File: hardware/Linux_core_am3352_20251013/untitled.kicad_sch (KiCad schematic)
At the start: 1 part, among them U1 AM3352BZCZ100

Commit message: update
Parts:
- removed U1: AM3352BZCZ100, My_Library:ZCZ0324A, symbol My_Library:AM3352BZCZ100
- added C1, C2: 18pF, symbol Device:C_Small
- added C3, C4: 22pF, symbol Device:C_Small
- added R1: R_Small, symbol Device:R_Small
- added R2, R3: 0Ω, symbol Device:R_Small
- added U1: AM3352BZCZ100, My_Library:ZCZ0324A, symbol My_Library:AM3352BZCZ100
- added Y1: 24MHz, Oscillator:Oscillator_SMD_Abracon_ASCO-4Pin_1.6x1.2mm, symbol Device:Crystal_GND24_Small
- added Y2: 32.768KHz, symbol Device:Crystal_Small
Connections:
- new net: C4.2, R3.1, Y2.1
- new net: C3.2, U1.A6 (RTC_XTALIN), Y2.2
- new net: C2.2, R1.2, R2.1, Y1.1
- new net: C1.2, R1.1, U1.V10 (XTALIN), Y1.3
- new net: R2.2, U1.U11 (XTALOUT)
- new net: R3.2, U1.A4 (RTC_XTALOUT)
- new net GND_OSC0: C1.1, C2.1, C3.1, C4.1, U1.A5 (VSS_RTC), U1.V11 (VSS_OSC)
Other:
- removed sheet am3352_a
- note added: "确认晶振接地方案"

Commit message: update
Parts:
- added C5: 0.1uF, symbol Device:C_Small
- added R4: 49.9Ω, symbol Device:R_Small
- added R5: 100KΩ, symbol Device:R_Small
- added R6, R7, R8: 10KΩ, symbol Device:R_Small
- added R9: 22Ω, symbol Device:R_Small
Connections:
- net at U1.A10 (WARMRST_N): now also R6.1
- net JTAG_TDO: now reaches U1.A11 (TDO)
- net JTAG_TCK: now reaches U1.A12 (TCK)
- net at U1.A15 (XDMA_EVENT_INTR0): now also R7.2
- net DDR_A5: now reaches U1.B1 (DDR_A5)
- net JTAG_TRST_N: now reaches U1.B10 (TRST_N)
- net JTAG_TDI: now reaches U1.B11 (TDI)
- net JTAG_EMU1: now reaches U1.B14 (EMU1)
- net PWRONRST_N: now reaches U1.B15 (PWRONRST_N)
- net PWRONRST_N: now also R5.2
- net EXTINT_N: now reaches U1.B18 (EXTINT_N)
- net DDR_WEn: now reaches U1.B2 (DDR_WE_N)
- net DDR_BA2: now reaches U1.B3 (DDR_BA2)
- net RTC_PORz: now reaches U1.B5 (RTC_PWRONRST_N)
- net DDR_A9: now reaches U1.C1 (DDR_A9)
- net JTAG_TMS: now reaches U1.C11 (TMS)
- net JTAG_EMU0: now reaches U1.C14 (EMU0)
- net DDR_A4: now reaches U1.C2 (DDR_A4)
- net DDR_A3: now reaches U1.C3 (DDR_A3)
- net DDR_BA0: now reaches U1.C4 (DDR_BA0)
- net DDR_CKn: now reaches U1.D1 (DDR_CK_N)
- net at U1.D14 (XDMA_EVENT_INTR1): now also R8.2
- net DDR_CK: now reaches U1.D2 (DDR_CK)
- net DDR_A15: now reaches U1.D3 (DDR_A15)
- net DDR_A8: now reaches U1.D4 (DDR_A8)
- net DDR_A6: now reaches U1.D5 (DDR_A6)
- net DDR_BA1: now reaches U1.E1 (DDR_BA1)
- net DDR_A7: now reaches U1.E2 (DDR_A7)
- net DDR_A12: now reaches U1.E3 (DDR_A12)
- net DDR_A2: now reaches U1.E4 (DDR_A2)
- net DDR_CASn: now reaches U1.F1 (DDR_CAS_N)
- net MMC0_DAT3: now reaches U1.F17 (MMC0_DAT3)
- net MMC0_DAT2: now reaches U1.F18 (MMC0_DAT2)
- net DDR_A11: now reaches U1.F2 (DDR_A11)
- net DDR_A0: now reaches U1.F3 (DDR_A0)
- net DDR_A10: now reaches U1.F4 (DDR_A10)
- net DDR_ODT: now reaches U1.G1 (DDR_ODT)
- net MMC0_DAT1: now reaches U1.G15 (MMC0_DAT1)
- net MMC0_DAT0: now reaches U1.G16 (MMC0_DAT0)
- net MMC0_CLK: now reaches U1.G17 (MMC0_CLK)
- net at U1.G18 (MMC0_CMD): now also R9.2
- net DDR_RESETn: now reaches U1.G2 (DDR_RESET_N)
- net DDR_CKE: now reaches U1.G3 (DDR_CKE)
- net DDR_RASn: now reaches U1.G4 (DDR_RAS_N)
- net DDR_A1: now reaches U1.H1 (DDR_A1)
- net DDR_CSn0: now reaches U1.H2 (DDR_CS0_N)
- net DDR_A13: now reaches U1.H3 (DDR_A13)
- net DDR_A14: now reaches U1.H4 (DDR_A14)
- net DDR_D8: now reaches U1.J1 (DDR_D8)
- net DDR_DQM1: now reaches U1.J2 (DDR_DQM1)
- net at U1.J3 (DDR_VTP): now also R4.2
- net DDR_VREF: now reaches U1.J4 (DDR_VREF)
- net DDR_VREF: now also C5.2
- net DDR_D9: now reaches U1.K1 (DDR_D9)
- net DDR_D10: now reaches U1.K2 (DDR_D10)
- net DDR_D11: now reaches U1.K3 (DDR_D11)
- net DDR_D12: now reaches U1.K4 (DDR_D12)
- net DDR_DQS1: now reaches U1.L1 (DDR_DQS1)
- net DDR_DQSn1: now reaches U1.L2 (DDR_DQS1_N)
- net DDR_D13: now reaches U1.L3 (DDR_D13)
- net DDR_D14: now reaches U1.L4 (DDR_D14)
- net DDR_D15: now reaches U1.M1 (DDR_D15)
- net DDR_DQM0: now reaches U1.M2 (DDR_DQM0)
- net DDR_D0: now reaches U1.M3 (DDR_D0)
- net DDR_D1: now reaches U1.M4 (DDR_D1)
- net DDR_D2: now reaches U1.N1 (DDR_D2)
- net DDR_D3: now reaches U1.N2 (DDR_D3)
- net DDR_D4: now reaches U1.N3 (DDR_D4)
- net DDR_D5: now reaches U1.N4 (DDR_D5)
- net DDR_DQS0: now reaches U1.P1 (DDR_DQS0)
- net DDR_DQSn0: now reaches U1.P2 (DDR_DQS0_N)
- net DDR_D6: now reaches U1.P3 (DDR_D6)
- net DDR_D7: now reaches U1.P4 (DDR_D7)
- net GPMC_AD13: now reaches U1.R12 (GPMC_AD13)
- net GPMC_A0: now reaches U1.R13 (GPMC_A0)
- net GPMC_A4: now reaches U1.R14 (GPMC_A4)
- net GPMC_ADV_ALE_N: now reaches U1.R7 (GPMC_ADV_ALE_N)
- net GPMC_AD2: now reaches U1.R8 (GPMC_AD2)
- net GPMC_AD6: now reaches U1.R9 (GPMC_AD6)
- net GPMC_AD9: now reaches U1.T10 (GPMC_AD9)
- net GPMC_AD10: now reaches U1.T11 (GPMC_AD10)
- net GPMC_AD12: now reaches U1.T12 (GPMC_AD12)
- net GPMC_CS3_N: now reaches U1.T13 (GPMC_CS3_N)
- net GPMC_A3: now reaches U1.T14 (GPMC_A3)
- net GPMC_A7: now reaches U1.T15 (GPMC_A7)
- net GPMC_A10: now reaches U1.T16 (GPMC_A10)
- net GPMC_WAIT0: now reaches U1.T17 (GPMC_WAIT0)
- net GPMC_BE0_CLE_N: now reaches U1.T6 (GPMC_BE0_CLE_N)
- net GPMC_OEN_RE_N: now reaches U1.T7 (GPMC_OEN_RE_N)
- net GPMC_AD3: now reaches U1.T8 (GPMC_AD3)
- net GPMC_AD7: now reaches U1.T9 (GPMC_AD7)
- net GPMC_AD8: now reaches U1.U10 (GPMC_AD8)
- net GPMC_AD11: now reaches U1.U12 (GPMC_AD11)
- net GPMC_AD15: now reaches U1.U13 (GPMC_AD15)
- net GPMC_A2: now reaches U1.U14 (GPMC_A2)
- net GPMC_A6: now reaches U1.U15 (GPMC_A6)
- net GPMC_A9: now reaches U1.U16 (GPMC_A9)
- net GPMC_WP_N: now reaches U1.U17 (GPMC_WP_N)
- net GPMC_BE1_N: now reaches U1.U18 (GPMC_BE1_N)
- net GPMC_WE_N: now reaches U1.U6 (GPMC_WE_N)
- net GPMC_AD0: now reaches U1.U7 (GPMC_AD0)
- net GPMC_AD4: now reaches U1.U8 (GPMC_AD4)
- net GPMC_CS1_N: now reaches U1.U9 (GPMC_CS1_N)
- net GPMC_CLK: now reaches U1.V12 (GPMC_CLK)
- net GPMC_AD14: now reaches U1.V13 (GPMC_AD14)
- net GPMC_A1: now reaches U1.V14 (GPMC_A1)
- net GPMC_A5: now reaches U1.V15 (GPMC_A5)
- net GPMC_A8: now reaches U1.V16 (GPMC_A8)
- net GPMC_A11: now reaches U1.V17 (GPMC_A11)
- net GPMC_CS0_N: now reaches U1.V6 (GPMC_CS0_N)
- net GPMC_AD1: now reaches U1.V7 (GPMC_AD1)
- net GPMC_AD5: now reaches U1.V8 (GPMC_AD5)
- net GPMC_CS2_N: now reaches U1.V9 (GPMC_CS2_N)
- new net GND: C5.1, R4.1, R5.1
- new net MMC0_CMD: R9.1
- new net VDDSHV6: R6.2
- new net XDMA_EVENT_INTR0: R7.1
- new net XDMA_EVENT_INTR1: R8.1
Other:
- moved on the sheet: C1, C2, C3, C4, R1, R2, R3, U1A, Y1, Y2

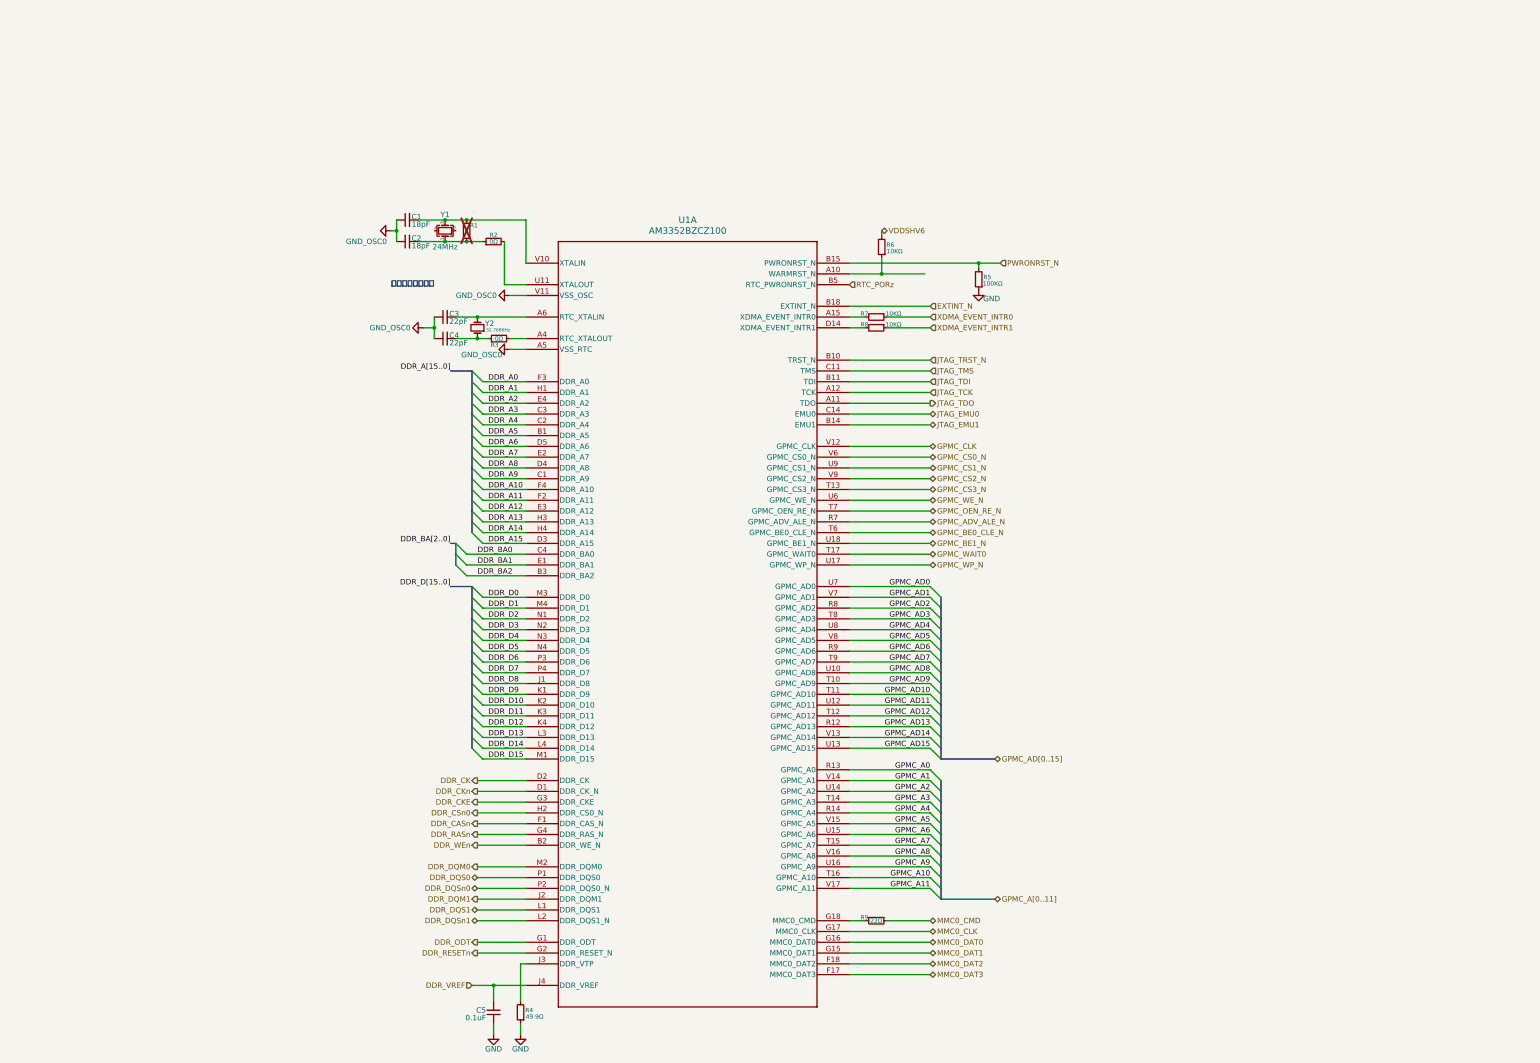
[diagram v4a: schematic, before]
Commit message: update schematic diagram
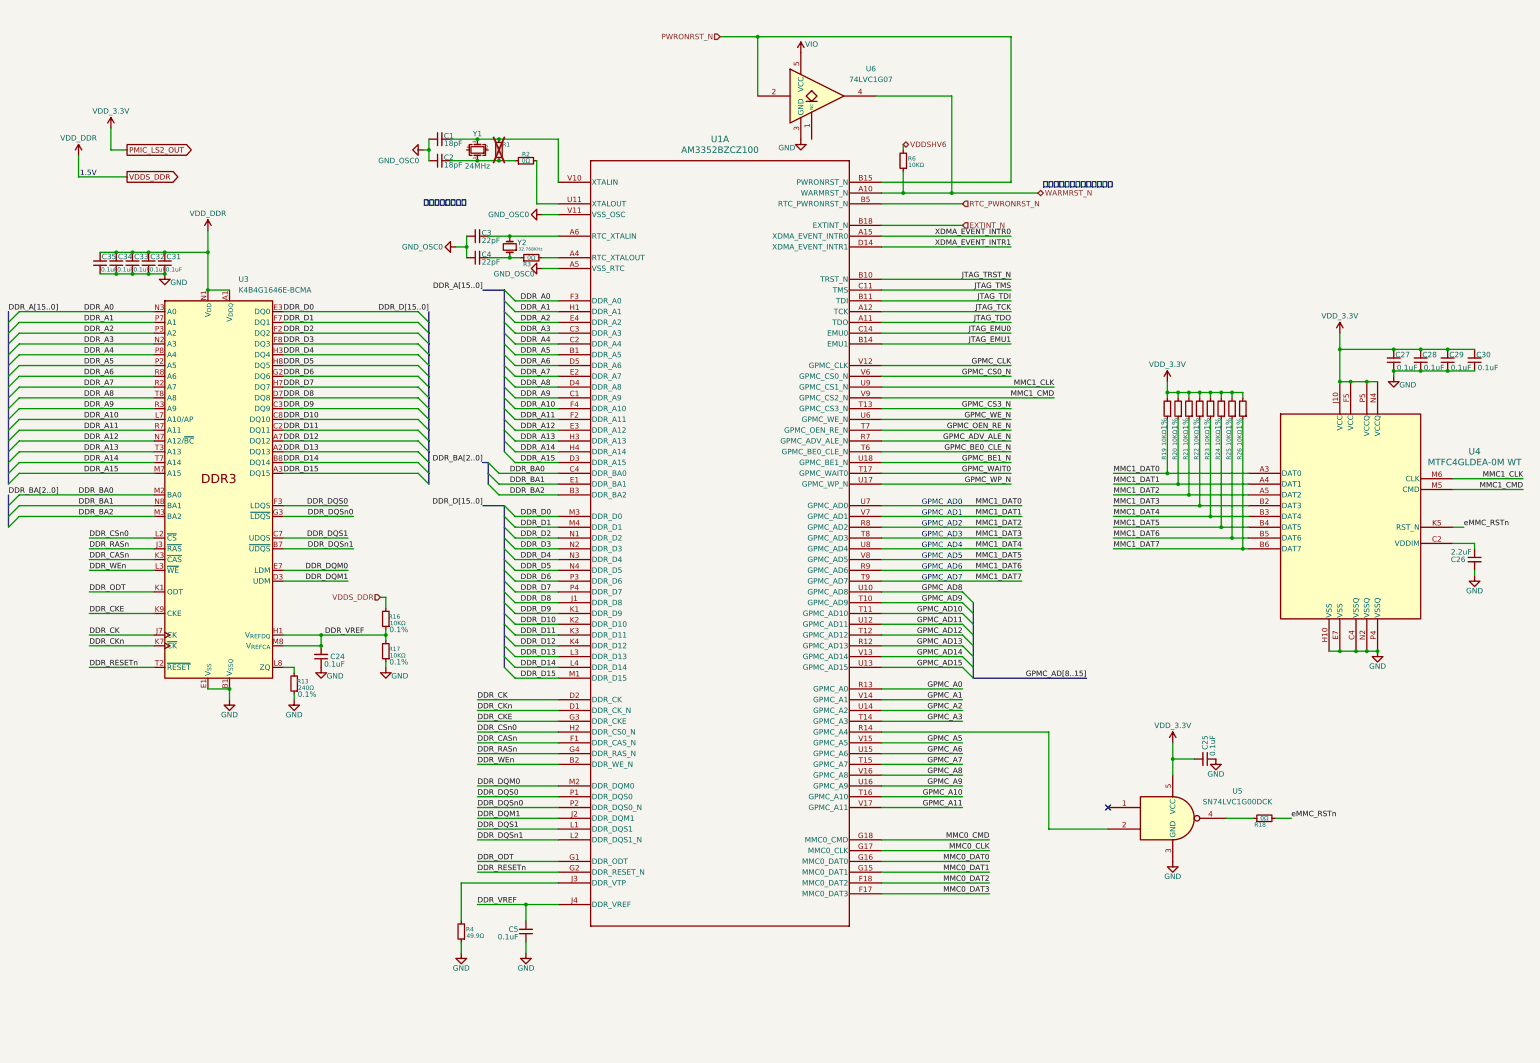
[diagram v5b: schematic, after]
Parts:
- removed R5: 100KΩ, symbol Device:R_Small
- removed R7, R8: 10KΩ, symbol Device:R_Small
- removed R9: 22Ω, symbol Device:R_Small
- added C24, C25, C27, C28, C29, C30, C31, C32, C33, C34, C35: 0.1uF, symbol Device:C_Small
- added C26: 2.2uF, symbol Device:C_Small
- added R13: 240Ω, symbol Device:R_Small
- added R16, R17, R19, R20, R21, R22, R23, R24, R25, R26: 10KΩ, symbol Device:R_Small
- added R18: 0Ω, symbol Device:R_Small
- added U3: K4B4G1646E-BCMA, Package_BGA:Micron_FBGA-96_7.5x13.5mm_Layout9x16_P0.8mm, symbol My_Library:K4B4G1646E
- added U4: MTFC4GLDEA-0M WT, Package_BGA:LFBGA-153_11.5x13mm_Layout14x14_P0.5mm, symbol My_Library:MTFC4GLDEA-0M_WT
- added U5: SN74LVC1G00DCK, Package_TO_SOT_SMD:Texas_R-PDSO-G5_DCK-5, symbol 74xGxx:SN74LVC1G00DCK
- added U6: 74LVC1G07, symbol 74xGxx:74LVC1G07
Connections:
- net DDR_A0: now also U3.N3 (A0)
- net DDR_A1: now also U3.P7 (A1)
- net DDR_A10: now also U3.L7 (A10/AP)
- net DDR_A11: now also U3.R7 (A11)
- net DDR_A12: now also U3.N7 (A12/~{BC})
- net DDR_A13: now also U3.T3 (A13)
- net DDR_A14: now also U3.T7 (A14)
- net DDR_A15: now also U3.M7 (A15)
- net DDR_A2: now also U3.P3 (A2)
- net DDR_A3: now also U3.N2 (A3)
- net DDR_A4: now also U3.P8 (A4)
- net DDR_A5: now also U3.P2 (A5)
- net DDR_A6: now also U3.R8 (A6)
- net DDR_A7: now also U3.R2 (A7)
- net DDR_A8: now also U3.T8 (A8)
- net DDR_A9: now also U3.R3 (A9)
- net DDR_BA0: now also U3.M2 (BA0)
- net DDR_BA1: now also U3.N8 (BA1)
- net DDR_BA2: now also U3.M3 (BA2)
- net DDR_CASn: now also U3.K3 (~{CAS})
- net DDR_CK: now also U3.J7 (CK)
- net DDR_CKE: now also U3.K9 (CKE)
- net DDR_CKn: now also U3.K7 (~{CK})
- net DDR_CSn0: now also U3.L2 (~{CS})
- net DDR_D0: now also U3.E3 (DQ0)
- net DDR_D1: now also U3.F7 (DQ1)
- net DDR_D10: now also U3.C8 (DQ10)
- net DDR_D11: now also U3.C2 (DQ11)
- net DDR_D12: now also U3.A7 (DQ12)
- net DDR_D13: now also U3.A2 (DQ13)
- net DDR_D14: now also U3.B8 (DQ14)
- net DDR_D15: now also U3.A3 (DQ15)
- net DDR_D2: now also U3.F2 (DQ2)
- net DDR_D3: now also U3.F8 (DQ3)
- net DDR_D4: now also U3.H3 (DQ4)
- net DDR_D5: now also U3.H8 (DQ5)
- net DDR_D6: now also U3.G2 (DQ6)
- net DDR_D7: now also U3.H7 (DQ7)
- net DDR_D8: now also U3.D7 (DQ8)
- net DDR_D9: now also U3.C3 (DQ9)
- net DDR_DQM0: now also U3.E7 (LDM)
- net DDR_DQM1: now also U3.D3 (UDM)
- net DDR_DQS0: now also U3.F3 (LDQS)
- net DDR_DQS1: now also U3.C7 (UDQS)
- net DDR_DQSn0: now also U3.G3 (~{LDQS})
- net DDR_DQSn1: now also U3.B7 (~{UDQS})
- net DDR_ODT: now also U3.K1 (ODT)
- net DDR_RASn: now also U3.J3 (~{RAS})
- net DDR_RESETn: now also U3.T2 (~{RESET})
- net DDR_VREF: now also C24.2, R16.1, R17.2, U3.H1 (V_{REFDQ}), U3.M8 (V_{REFCA})
- net DDR_WEn: now also U3.L3 (~{WE})
- net GND: now also C24.1, C25.1, C26.2, C27.1, C28.1, C29.1, C30.1, C31.1, C32.1, C33.1, C34.1, C35.1, R13.1, R17.1, U3.A9 (V_{SS}), U3.B1 (V_{SSQ}), U3.B3 (V_{SS}), U3.B9 (V_{SSQ}), U3.D1 (V_{SSQ}), U3.D8 (V_{SSQ}), U3.E1 (V_{SS}), U3.E2 (V_{SSQ}), U3.E8 (V_{SSQ}), U3.F9 (V_{SSQ}), U3.G1 (V_{SSQ}), U3.G8 (V_{SS}), U3.G9 (V_{SSQ}), U3.J2 (V_{SS}), U3.J8 (V_{SS}), U3.M1 (V_{SS}), U3.M9 (V_{SS}), U3.P1 (V_{SS}), U3.P9 (V_{SS}), U3.T1 (V_{SS}), U3.T9 (V_{SS}), U4.C4 (VSSQ), U4.E7 (VSS), U4.G5 (VSS), U4.H10 (VSS), U4.K8 (VSS), U4.N2 (VSSQ), U4.N5 (VSSQ), U4.P4 (VSSQ), U4.P6 (VSSQ), U5.3 (GND), U6.3 (GND)
- net MMC0_CMD: now also U1.G18 (MMC0_CMD)
- net PWRONRST_N: now also U6.2
- net XDMA_EVENT_INTR0: now also U1.A15 (XDMA_EVENT_INTR0)
- net XDMA_EVENT_INTR1: now also U1.D14 (XDMA_EVENT_INTR1)
- net WARMRST_N: now reaches R6.1, U1.A10 (WARMRST_N)
- net WARMRST_N: now also U6.4
- net GPMC_A4: no longer names the net of U1.R14 (GPMC_A4)
- net GPMC_A4: now also U5.2
- net GPMC_AD0 renamed MMC1_DAT0
- net MMC1_DAT0: now also R19.1, U4.A3 (DAT0)
- net GPMC_AD1 renamed MMC1_DAT1
- net MMC1_DAT1: now also R20.1, U4.A4 (DAT1)
- net GPMC_AD2 renamed MMC1_DAT2
- net MMC1_DAT2: now also R21.1, U4.A5 (DAT2)
- net GPMC_AD3 renamed MMC1_DAT3
- net MMC1_DAT3: now also R22.1, U4.B2 (DAT3)
- net GPMC_AD4 renamed MMC1_DAT4
- net MMC1_DAT4: now also R23.1, U4.B3 (DAT4)
- net GPMC_AD5 renamed MMC1_DAT5
- net MMC1_DAT5: now also R24.1, U4.B4 (DAT5)
- net GPMC_AD6 renamed MMC1_DAT6
- net MMC1_DAT6: now also R25.1, U4.B5 (DAT6)
- net GPMC_AD7 renamed MMC1_DAT7
- net MMC1_DAT7: now also R26.1, U4.B6 (DAT7)
- net GPMC_CS1_N renamed MMC1_CLK
- net MMC1_CLK: now also U4.M6 (CLK)
- net GPMC_CS2_N renamed MMC1_CMD
- net MMC1_CMD: now also U4.M5 (CMD)
- net RTC_PORz renamed RTC_PWRONRST_N
- new net: R13.2, U3.L8 (ZQ)
- new net: R18.1, U5.4
- new net: U4.A1 (NC), U4.A10 (NC), U4.A11 (NC), U4.A12 (NC), U4.A13 (NC), U4.A14 (NC), U4.A2 (NC), U4.A8 (NC), U4.A9 (NC), U4.B1 (NC), U4.B10 (NC), U4.B11 (NC), U4.B12 (NC), U4.B13 (NC), U4.B14 (NC), U4.B7 (NC), U4.B8 (NC), U4.B9 (NC), U4.C1 (NC), U4.C10 (NC), U4.C11 (NC), U4.C12 (NC), U4.C13 (NC), U4.C14 (NC), U4.C3 (NC), U4.C7 (NC), U4.C8 (NC), U4.C9 (NC), U4.D1 (NC), U4.D12 (NC), U4.D13 (NC), U4.D14 (NC), U4.D2 (NC), U4.D3 (NC), U4.D4 (NC), U4.E1 (NC), U4.E12 (NC), U4.E13 (NC), U4.E14 (NC), U4.E2 (NC), U4.E3 (NC), U4.F12 (NC), U4.F13 (NC), U4.F14 (NC), U4.G12 (NC), U4.G13 (NC), U4.G14 (NC), U4.H12 (NC), U4.H13 (NC), U4.H14 (NC), U4.J12 (NC), U4.J13 (NC), U4.J14 (NC), U4.K12 (NC), U4.K13 (NC), U4.K14 (NC), U4.L12 (NC), U4.L13 (NC), U4.L14 (NC), U4.M10 (NC), U4.M11 (NC), U4.M12 (NC), U4.M13 (NC), U4.M14 (NC), U4.N10 (NC), U4.N11 (NC), U4.N12 (NC), U4.N13 (NC), U4.N14 (NC), U4.N3 (NC), U4.N6 (NC), U4.N7 (NC), U4.N8 (NC), U4.N9 (NC), U4.P1 (NC), U4.P11 (NC), U4.P12 (NC), U4.P13 (NC), U4.P14 (NC), U4.P2 (NC), U4.P8 (NC), U4.P9 (NC)
- new net: U4.A6 (RFU), U4.A7 (RFU), U4.C5 (RFU), U4.E5 (RFU), U4.E8 (RFU)
- new net: C26.1, U4.C2 (VDDIM)
- new net: U4.E10 (RFU), U4.E9 (RFU), U4.F10 (RFU), U4.G10 (RFU), U4.G3 (RFU), U4.H5 (RFU), U4.J5 (RFU), U4.K10 (RFU), U4.K6 (RFU), U4.K7 (RFU), U4.P10 (RFU), U4.P7 (RFU)
- new net: U4.F1 (NC), U4.F2 (NC), U4.F3 (NC), U4.G1 (NC), U4.G2 (NC), U4.H1 (NC), U4.H2 (NC), U4.H3 (NC), U4.J1 (NC), U4.J2 (NC), U4.J3 (NC), U4.K1 (NC), U4.K2 (NC), U4.K3 (NC), U4.L1 (NC), U4.L2 (NC), U4.L3 (NC), U4.M1 (NC), U4.M2 (NC), U4.M3 (NC), U4.M7 (NC), U4.M8 (NC), U4.M9 (NC), U4.N1 (NC)
- new net VCC: C25.2, C27.2, C28.2, C29.2, C30.2, R19.2, R20.2, R21.2, R22.2, R23.2, R24.2, R25.2, R26.2, U4.C6 (VCCQ), U4.E6 (VCC), U4.F5 (VCC), U4.J10 (VCC), U4.K9 (VCC), U4.M4 (VCCQ), U4.N4 (VCCQ), U4.P3 (VCCQ), U4.P5 (VCCQ), U5.5 (VCC)
- new net VDD_DDR: C31.2, C32.2, C33.2, C34.2, C35.2, R16.2, U3.A1 (V_{DDQ}), U3.A8 (V_{DDQ}), U3.B2 (V_{DD}), U3.C1 (V_{DDQ}), U3.C9 (V_{DDQ}), U3.D2 (V_{DDQ}), U3.D9 (V_{DD}), U3.E9 (V_{DDQ}), U3.F1 (V_{DDQ}), U3.G7 (V_{DD}), U3.H2 (V_{DDQ}), U3.H9 (V_{DDQ}), U3.K2 (V_{DD}), U3.K8 (V_{DD}), U3.N1 (V_{DD}), U3.N9 (V_{DD}), U3.R1 (V_{DD}), U3.R9 (V_{DD})
- new net VIO: U6.5 (VCC)
- new net eMMC_RSTn: R18.2, U4.K5 (RST_N)
- no-connect marks 0 -> 1
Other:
- note added: "1.5V"
- note added: "GPMC_AD0"
- note added: "GPMC_AD1"
- note added: "GPMC_AD2"
- note added: "GPMC_AD3"
- note added: "GPMC_AD4"
- note added: "GPMC_AD5"
- note added: "GPMC_AD6"
- note added: "GPMC_AD7"
- note added: "留作外部引出引脚，用作重启"
- moved on the sheet: C1, C2, C3, C4, C5, R1, R2, R3, R4, R6, U1A, Y1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
